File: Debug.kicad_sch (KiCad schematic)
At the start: 10 parts, among them J1 USB_C_Receptacle_USB2.0_14P, U3 CH340C

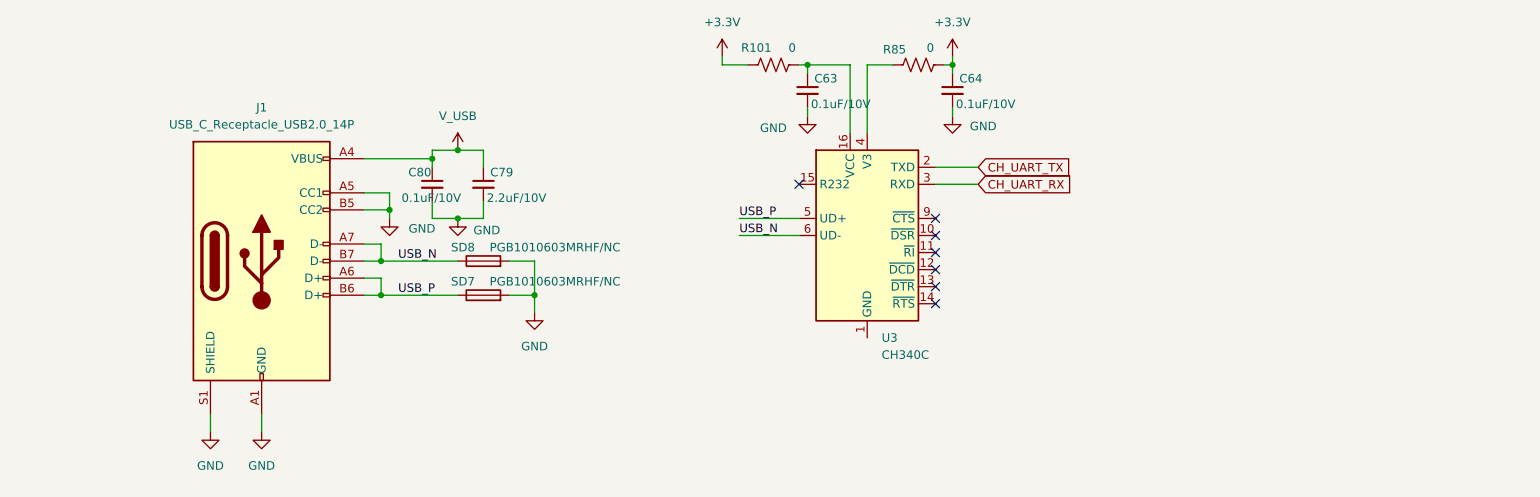
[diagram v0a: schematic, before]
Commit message: All footprints configured correctly. Next step is layout
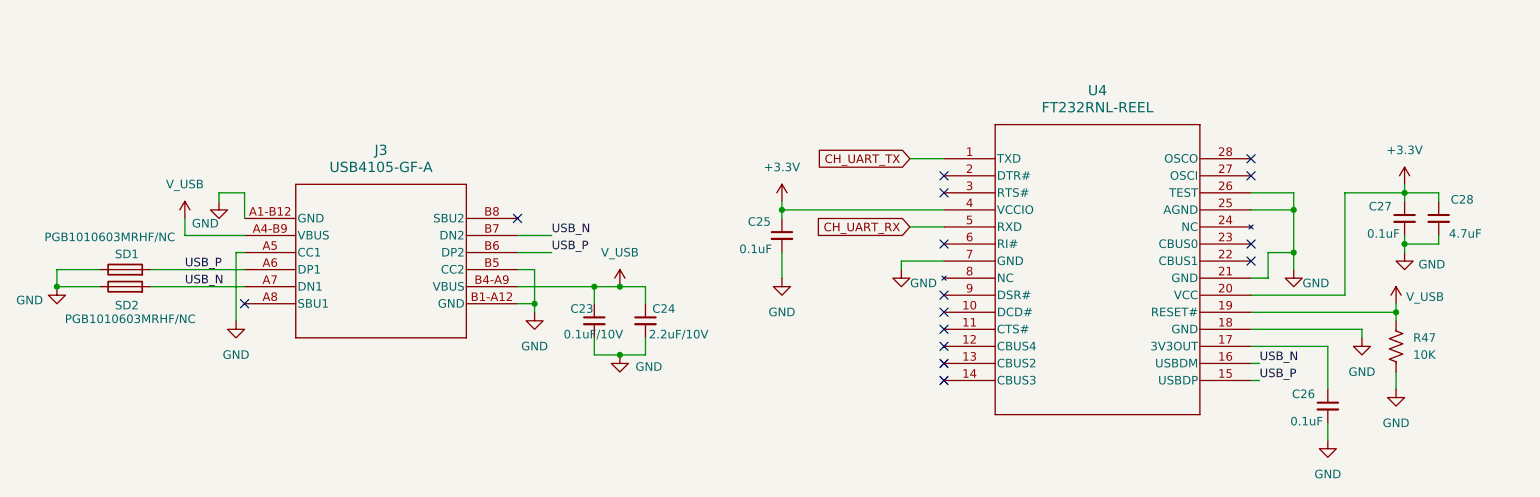
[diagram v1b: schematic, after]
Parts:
- removed C63, C64: 0.1uF/10V, symbol Device:C_Small
- removed J1: USB_C_Receptacle_USB2.0_14P, symbol Connector:USB_C_Receptacle_USB2.0_14P
- removed R101, R85: 0, symbol Device:R_US
- removed U3: CH340C, Package_SO:SOIC-16_3.9x9.9mm_P1.27mm, symbol Interface_USB:CH340C
- added C25, C26, C27: 0.1uF, Capacitor_SMD:C_0201_0603Metric_Pad0.64x0.40mm_HandSolder, symbol Device:C_Small
- added C28: 4.7uF, Capacitor_SMD:C_0201_0603Metric_Pad0.64x0.40mm_HandSolder, symbol Device:C_Small
- added J3: USB4105-GF-A, USB4105_GCT, symbol 2026-01-20_11-05-16:USB4105-GF-A
- added R47: 10K, Resistor_SMD:R_0201_0603Metric_Pad0.64x0.40mm_HandSolder, symbol Device:R_US
- added U4: FT232RNL-REEL, SSOP-28_FTD, symbol 2026-01-18_17-37-00:FT232RNL-REEL
- C23: renamed from C80; footprint (none) -> Capacitor_SMD:C_0201_0603Metric_Pad0.64x0.40mm_HandSolder
- C24: renamed from C79; footprint (none) -> Capacitor_SMD:C_0201_0603Metric_Pad0.64x0.40mm_HandSolder
- renumbered SD7 to SD1, SD8 to SD2
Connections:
- net +3.3V: now also C25.1, C27.1, C28.1, U4.20 (VCC), U4.4 (VCCIO)
- net CH_UART_RX: now also U4.5 (RXD)
- net CH_UART_TX: now also U4.1 (TXD)
- net GND: now also SD1.1, SD2.1, C25.2, C26.2, C27.2, C28.2, J3.A1-B12 (GND), J3.A5 (CC1), J3.B1-A12 (GND), J3.B5 (CC2), R47.2, U4.18 (GND), U4.21 (GND), U4.25 (AGND), U4.26 (TEST), U4.7 (GND); no longer SD1.2, SD2.2
- net USB_N: now also SD2.2, J3.A7 (DN1), J3.B7 (DN2), U4.16 (USBDM); no longer SD2.1
- net USB_P: now also SD1.2, J3.A6 (DP1), J3.B6 (DP2), U4.15 (USBDP); no longer SD1.1
- net V_USB: now also J3.A4-B9 (VBUS), J3.B4-A9 (VBUS), R47.1, U4.19 (RESET#)
- new net: C26.1, U4.17 (3V3OUT)
- no-connect marks 7 -> 15
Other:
- moved on the sheet: C23, C24, SD1, SD2

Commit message: In the middle of layout. WIP
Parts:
- C23: value 0.1uF/10V -> 0.1uF
- C24: value 2.2uF/10V -> 2.2uF
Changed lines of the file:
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@@
 			)
 		)
-		(property "Value" "2.2uF/10V"
+		(property "Value" "2.2uF"
 			(at 108.458 62.992 0)
 			(effects
@@
 			)
 		)
-		(property "Value" "0.1uF/10V"
+		(property "Value" "0.1uF"
 			(at 95.758 62.992 0)
 			(effects

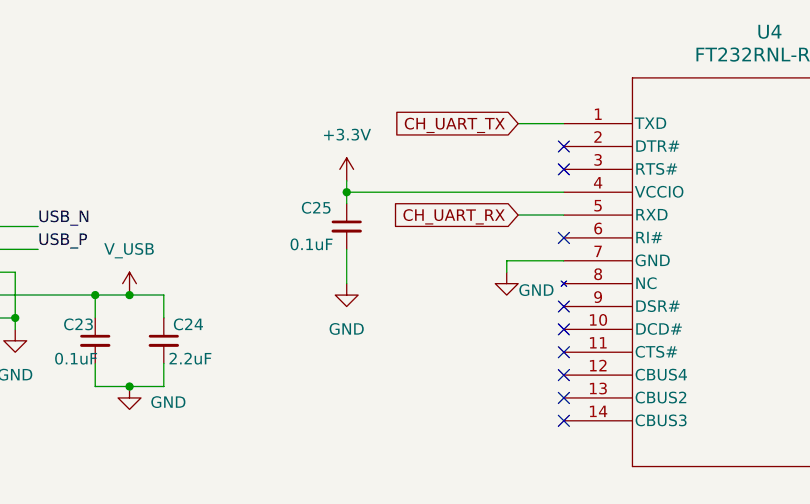
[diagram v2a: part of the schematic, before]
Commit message: Added 1k resistors in series with the FTDI Tx & Rx lines. This was recommended by Gemini to protect when the VCC is unpowered to the FTDI chip, and we're running from battery.
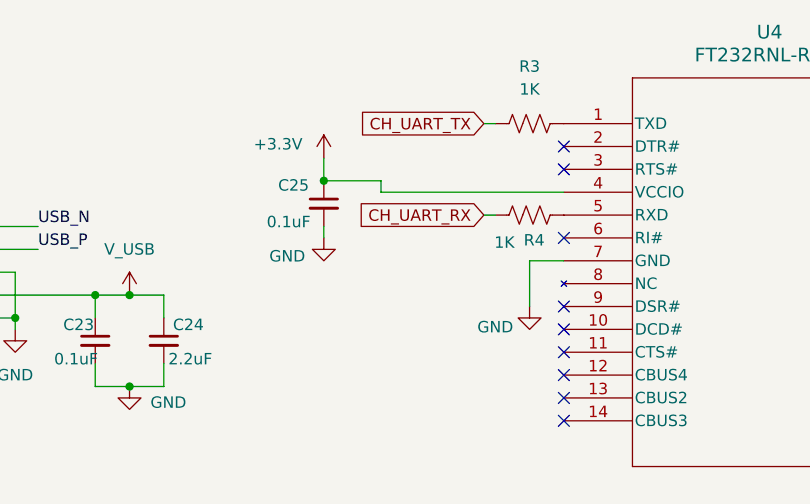
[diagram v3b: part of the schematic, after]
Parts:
- added R3, R4: 1K, Resistor_SMD:R_0201_0603Metric_Pad0.64x0.40mm_HandSolder, symbol Device:R_US
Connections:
- net CH_UART_RX: now also R4.1; no longer U4.5 (RXD)
- net CH_UART_TX: now also R3.2; no longer U4.1 (TXD)
- new net: R4.2, U4.5 (RXD)
- new net: R3.1, U4.1 (TXD)
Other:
- moved on the sheet: C25

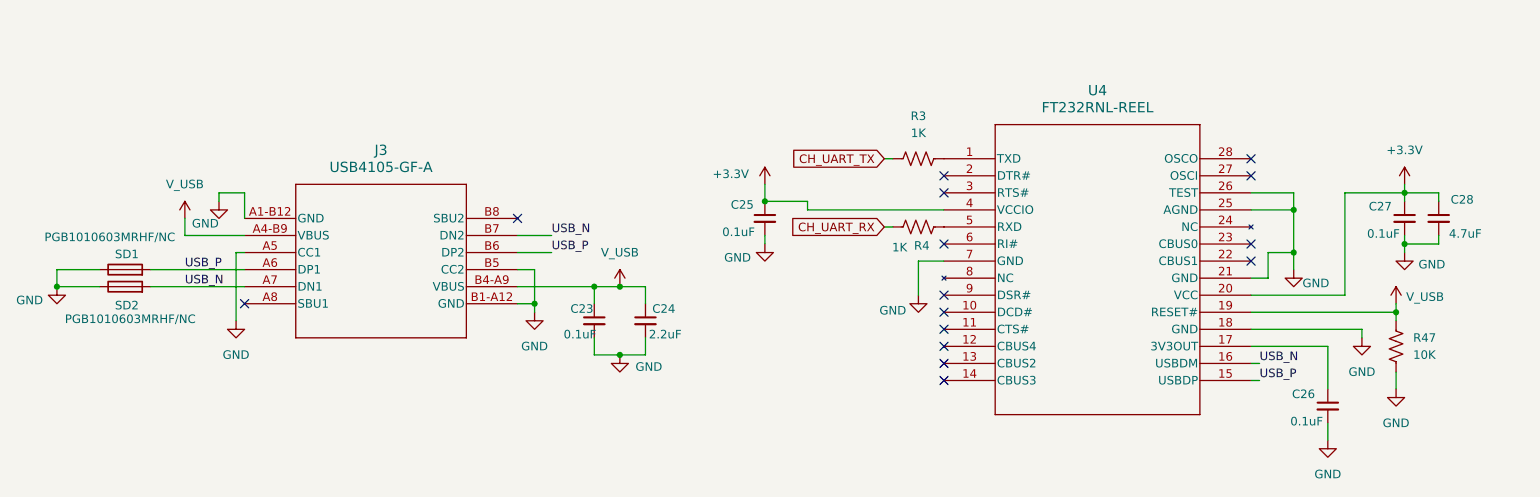
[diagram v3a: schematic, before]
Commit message: Replaced all passive footprints from 0603 metric to 0603 imperial. Big oversight. All done. Next is DRC
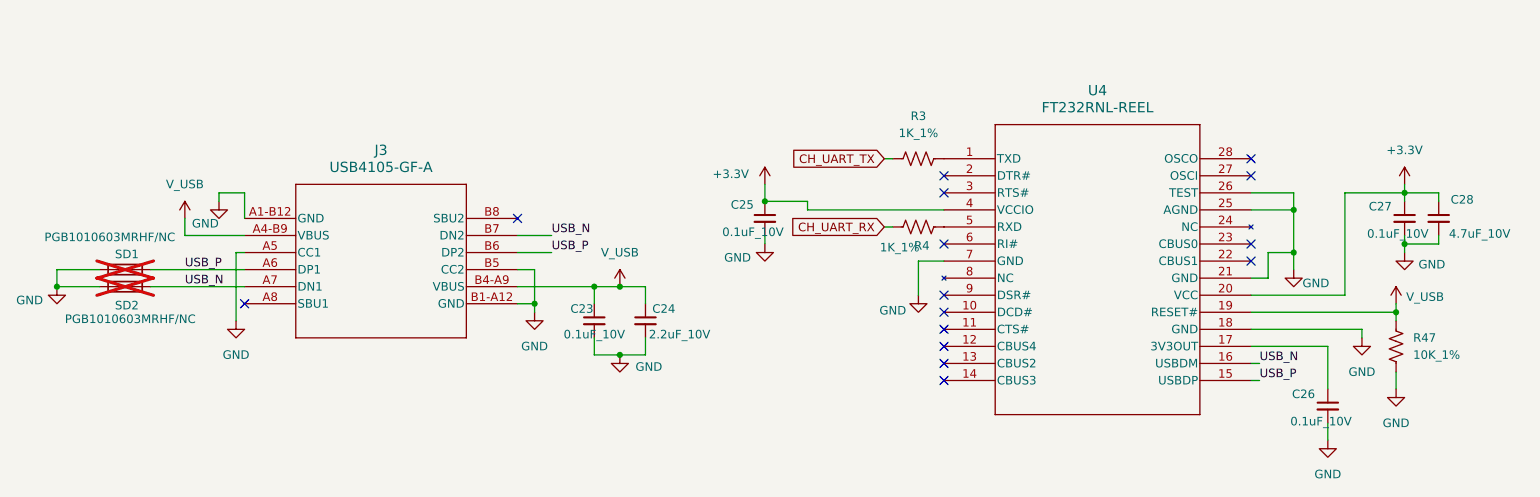
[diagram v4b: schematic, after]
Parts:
- C23, C25, C26, C27: value 0.1uF -> 0.1uF_10V; footprint Capacitor_SMD:C_0201_0603Metric_Pad0.64x0.40mm_HandSolder -> Capacitor_SMD:C_0603_1608Metric
- C24: value 2.2uF -> 2.2uF_10V; footprint Capacitor_SMD:C_0201_0603Metric_Pad0.64x0.40mm_HandSolder -> Capacitor_SMD:C_0603_1608Metric
- C28: value 4.7uF -> 4.7uF_10V; footprint Capacitor_SMD:C_0201_0603Metric_Pad0.64x0.40mm_HandSolder -> Capacitor_SMD:C_0603_1608Metric
- R3, R4: value 1K -> 1K_1%; footprint Resistor_SMD:R_0201_0603Metric_Pad0.64x0.40mm_HandSolder -> Resistor_SMD:R_0603_1608Metric
- R47: value 10K -> 10K_1%; footprint Resistor_SMD:R_0201_0603Metric_Pad0.64x0.40mm_HandSolder -> Resistor_SMD:R_0603_1608Metric
- SD1, SD2: now not fitted
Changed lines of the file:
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@@
 			)
 		)
-		(property "Value" "1K"
+		(property "Value" "1K_1%"
 			(at 145.796 50.038 90)
 			(effects
@@
 			)
 		)
-		(property "Footprint" "Resistor_SMD:R_0201_0603Metric_Pad0.64x0.40mm_HandSolder"
+		(property "Footprint" "Resistor_SMD:R_0603_1608Metric"
 			(at 148.844 45.974 90)
 			(effects
@@
 			)
 		)
-		(property "Value" "0.1uF"
+		(property "Value" "0.1uF_10V"
 			(at 203.962 75.946 0)
 			(effects
@@
 			)
 		)
-		(property "Footprint" "Capacitor_SMD:C_0201_0603Metric_Pad0.64x0.40mm_HandSolder"
+		(property "Footprint" "Capacitor_SMD:C_0603_1608Metric"
 			(at 209.55 73.66 0)
 			(effects
@@
 		(in_bom yes)
 		(on_board yes)
-		(dnp no)
+		(dnp yes)
 		(property "Reference" "SD1"
 			(at 30.734 51.054 90)
@@
 			)
 		)
-		(property "Value" "10K"
+		(property "Value" "10K_1%"
 			(at 222.25 66.0399 0)
 			(effects
@@
 			)
 		)
-		(property "Footprint" "Resistor_SMD:R_0201_0603Metric_Pad0.64x0.40mm_HandSolder"
+		(property "Footprint" "Resistor_SMD:R_0603_1608Metric"
 			(at 220.726 65.024 90)
 			(effects
@@
 			)
 		)
-		(property "Value" "2.2uF"
+		(property "Value" "2.2uF_10V"
 			(at 108.458 62.992 0)
 			(effects
@@
 			)
 		)
-		(property "Footprint" "Capacitor_SMD:C_0201_0603Metric_Pad0.64x0.40mm_HandSolder"
+		(property "Footprint" "Capacitor_SMD:C_0603_1608Metric"
 			(at 107.95 60.96 0)
 			(effects
@@
 		(in_bom yes)
 		(on_board yes)
-		(dnp no)
+		(dnp yes)
 		(property "Reference" "SD2"
 			(at 30.734 58.674 90)
@@
 			)
 		)
-		(property "Value" "0.1uF"
+		(property "Value" "0.1uF_10V"
 			(at 215.392 48.006 0)
 			(effects
@@
 			)
 		)
-		(property "Footprint" "Capacitor_SMD:C_0201_0603Metric_Pad0.64x0.40mm_HandSolder"
+		(property "Footprint" "Capacitor_SMD:C_0603_1608Metric"
 			(at 220.98 45.72 0)
 			(effects
@@
 			)
 		)
-		(property "Value" "1K"
+		(property "Value" "1K_1%"
 			(at 148.59 33.02 90)
 			(effects
@@
 			)
 		)
-		(property "Footprint" "Resistor_SMD:R_0201_0603Metric_Pad0.64x0.40mm_HandSolder"
+		(property "Footprint" "Resistor_SMD:R_0603_1608Metric"
 			(at 148.336 37.846 90)
 			(effects
@@
 			)
 		)
-		(property "Value" "0.1uF"
+		(property "Value" "0.1uF_10V"
 			(at 95.758 62.992 0)
 			(effects
@@
 			)
 		)
-		(property "Footprint" "Capacitor_SMD:C_0201_0603Metric_Pad0.64x0.40mm_HandSolder"
+		(property "Footprint" "Capacitor_SMD:C_0603_1608Metric"
 			(at 100.33 60.96 0)
 			(effects
@@
 			)
 		)
-		(property "Value" "4.7uF"
+		(property "Value" "4.7uF_10V"
 			(at 227.584 48.006 0)
 			(effects
@@
 			)
 		)
-		(property "Footprint" "Capacitor_SMD:C_0201_0603Metric_Pad0.64x0.40mm_HandSolder"
+		(property "Footprint" "Capacitor_SMD:C_0603_1608Metric"
 			(at 226.06 45.72 0)
 			(effects
@@
 			)
 		)
-		(property "Value" "0.1uF"
+		(property "Value" "0.1uF_10V"
 			(at 119.38 47.752 0)
 			(effects
@@
 			)
 		)
-		(property "Footprint" "Capacitor_SMD:C_0201_0603Metric_Pad0.64x0.40mm_HandSolder"
+		(property "Footprint" "Capacitor_SMD:C_0603_1608Metric"
 			(at 125.73 45.72 0)
 			(effects

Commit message: All fiducials and mounting holes placed. Except one hole, which I'll try to place. WIP
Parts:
- J3: footprint USB4105_GCT -> USB4105-GF-A:USB4105_GCT
- U4: footprint SSOP-28_FTD -> FT232RNL:SSOP-28_FTD
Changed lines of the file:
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@@
 			)
 		)
-		(property "Footprint" "USB4105_GCT"
+		(property "Footprint" "USB4105-GF-A:USB4105_GCT"
 			(at 48.26 45.72 0)
 			(effects
@@
 			)
 		)
-		(property "Footprint" "SSOP-28_FTD"
+		(property "Footprint" "FT232RNL:SSOP-28_FTD"
 			(at 152.4 36.83 0)
 			(effects
